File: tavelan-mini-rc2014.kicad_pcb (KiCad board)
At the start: 2 copper layers, 132 x 112 mm, 28 parts, among them J1 Alternate_Reset, J2 Regulated_Power, SW1 Reset

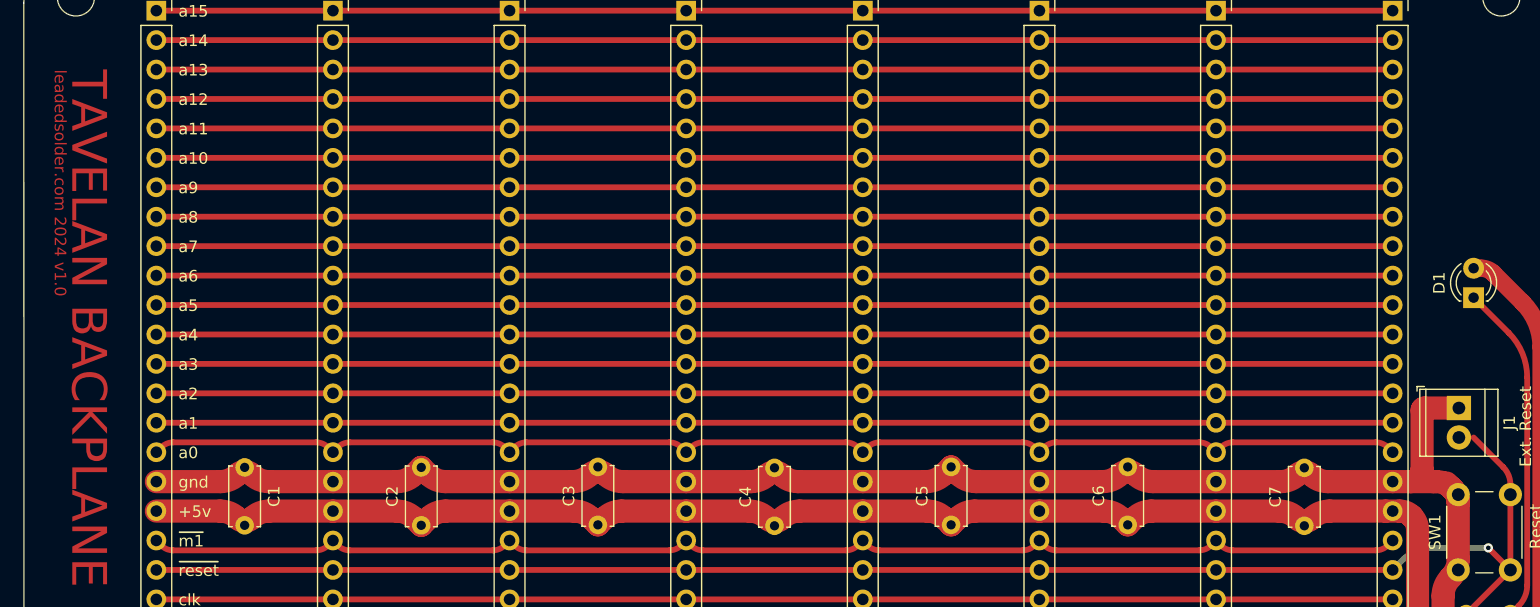
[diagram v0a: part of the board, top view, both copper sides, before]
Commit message: Add 5V and GND traces to the back, too
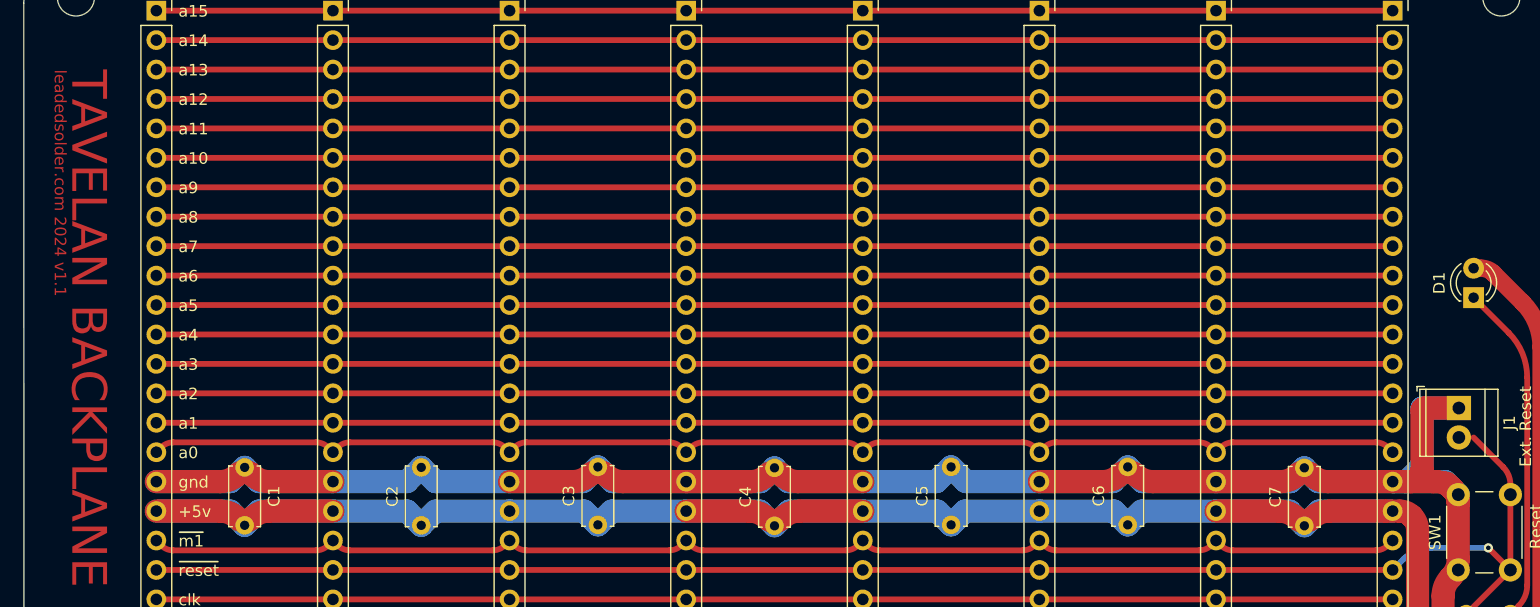
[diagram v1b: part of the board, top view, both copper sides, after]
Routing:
- net GND: track 188.0 -> 287.1 mm
- net +5V: track 219.1 -> 268.7 mm
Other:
- board text added: "leadedsolder.com 2024 v1.1"

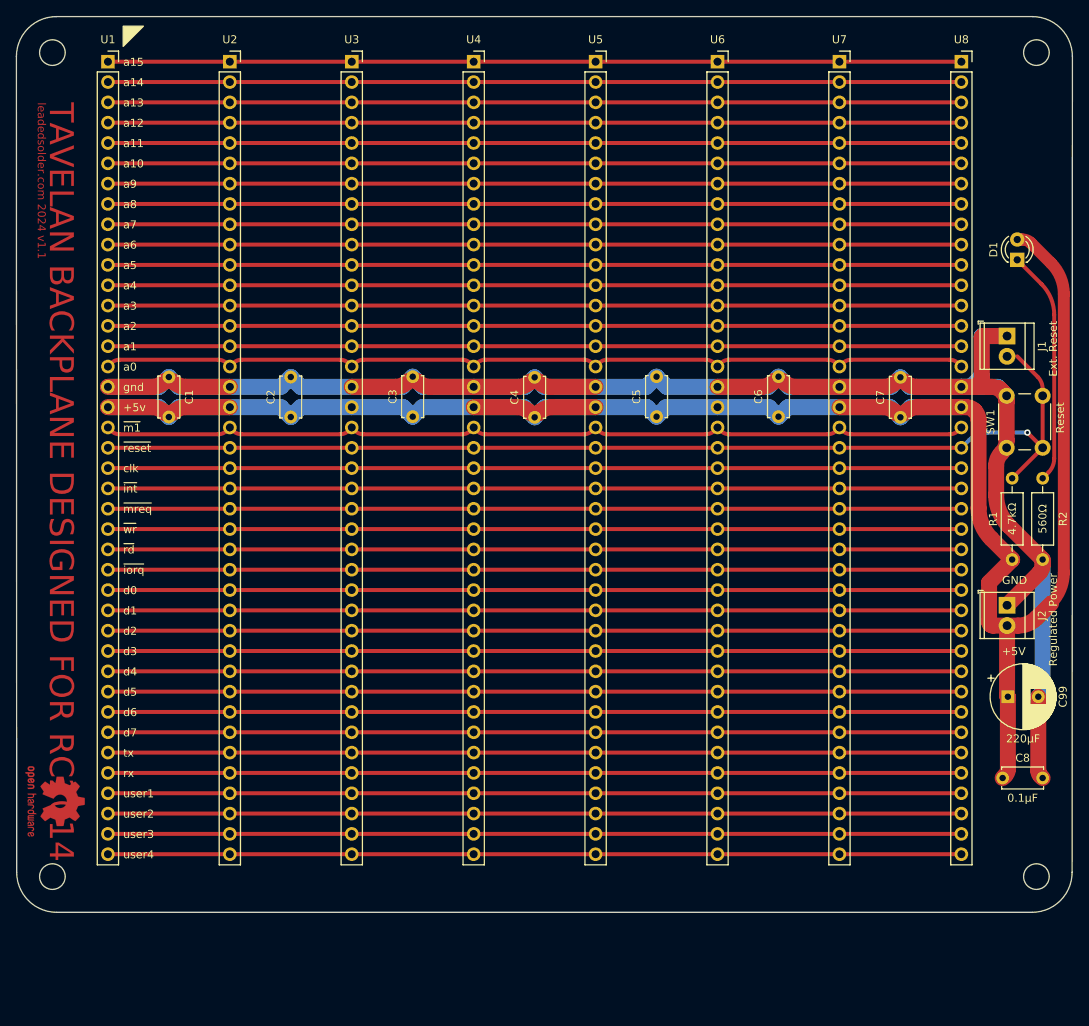
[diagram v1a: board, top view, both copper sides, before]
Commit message: Route reset trace in a way that doesn't screw up power
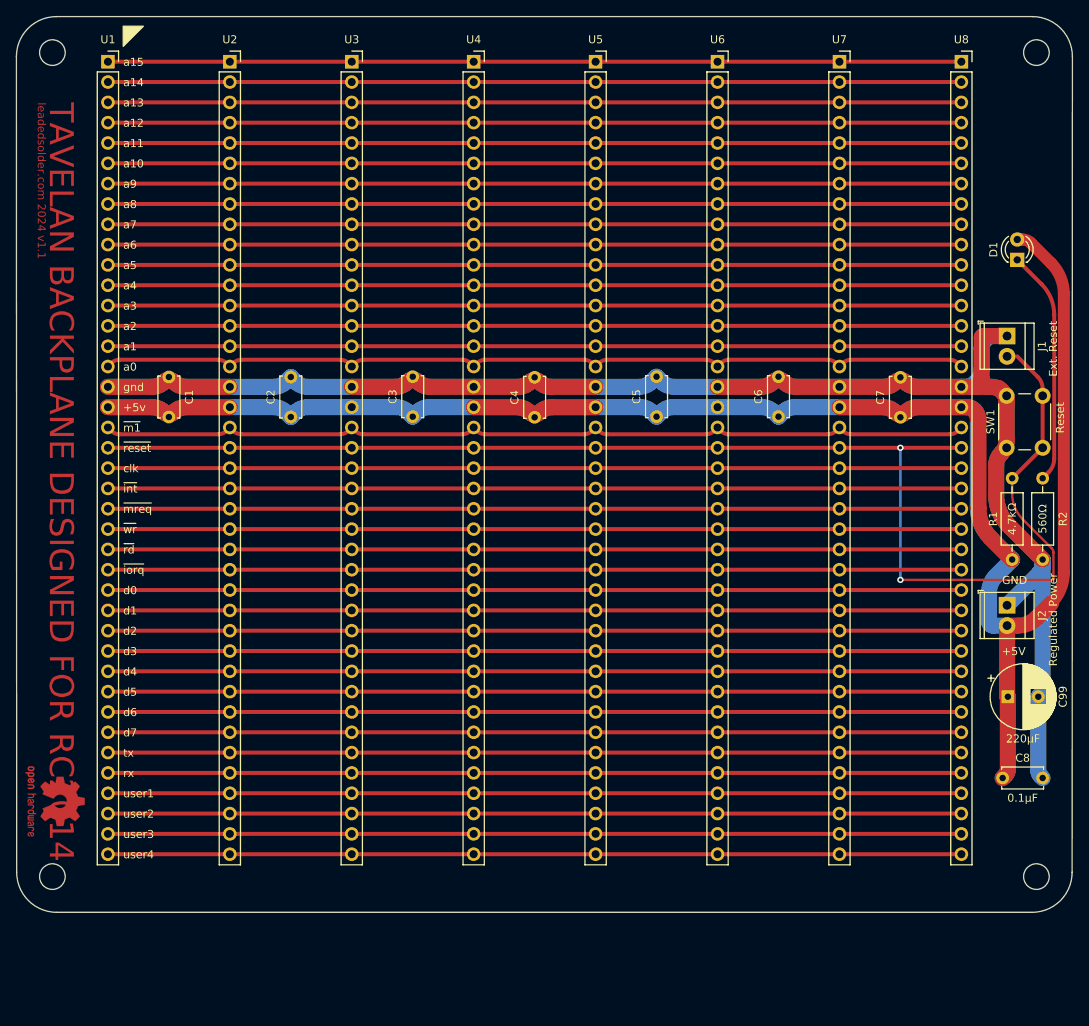
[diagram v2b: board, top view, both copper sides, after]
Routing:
- net /~{RESET}: track 136.3 -> 174.9 mm, vias 1 -> 2
- net +5V: track 268.7 -> 307.2 mm
- net GND: track 287.1 -> 305.4 mm

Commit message: Ground pour; add power switch header
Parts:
- added J3: Power_SW, TerminalBlock_TE-Connectivity:TerminalBlock_TE_282834-2_1x02_P2.54mm_Horizontal, F.Cu at (205.7, 134.6)
- moved C8 22.2 mm to (203.8, 108.0)
- moved J2 16.6 mm to (205.7, 125.1)
- moved C99 3.81 mm to (203.9, 116.2)
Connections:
- J2 pad 2: +5V -> Net-(J2-Pin_2)
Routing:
- net GND: track 305.4 -> 270.8 mm
- net +5V: track 307.2 -> 292.9 mm
- net Net-(J2-Pin_2): track 0.00 -> 12.1 mm
- added copper zone on B.Cu, net GND
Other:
- board text removed: "leadedsolder.com 2024 v1.0"
